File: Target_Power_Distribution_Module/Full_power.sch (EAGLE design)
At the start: 26 parts, among them IC1 MCP1702, Q1 NFET, Q2 PFET, Q3 NFET, Q4 PFET

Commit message: Initial .brd done for power
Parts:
- removed BAT1: 5V, SparkFun-Connectors:BC9VPC
- removed U$1: USB-CON-5PIN-105017-0001, GeekAmmo:USB-CON-5PIN-105017-0001
- added JP1: USB-MICROB, SparkFun-Connectors:USB-MICROB
- added PI, SENSOR, STATE_CONTROLLER: (no value), SparkFun-Connectors:M02PTH
- C1: device SparkFun-Capacitors:CAP1206 -> SparkFun-Passives:CAPPTH
- D1: device adafruit:SCHOTTKY-DIODECB429-15 -> SparkFun-DiscreteSemi:DIODEPTH
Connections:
- net 5V: now also STATE_CONTROLLER.1
- net 5V_RAW: now also JP1.VBUS; no longer BAT1.V+, U$1.VBUS
- net GND-ISO: now also JP1.GND, PI.2, SENSOR.2, STATE_CONTROLLER.2; no longer BAT1.V-, U$1.GND
- net PI_5V: now also PI.1
- net SENSOR_POWER: now also SENSOR.1
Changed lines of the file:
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@@
 <part name="R2" library="SparkFun-Resistors" deviceset="RESISTOR" device="1206" value="10k"/>
 <part name="R3" library="SparkFun-Resistors" deviceset="RESISTOR" device="1206" value="10k"/>
-<part name="D1" library="adafruit" deviceset="SCHOTTKY-DIODE" device="CB429-15" value="1N5817"/>
+<part name="D1" library="SparkFun-DiscreteSemi" deviceset="DIODE" device="PTH" value="1N5817"/>
 <part name="F1" library="fuse" deviceset="FUSE" device="PICOFUSE" value="2A"/>
 <part name="Q3" library="User-Submitted" deviceset="MOSFET-PCHANNEL" device="FQP27P06" value="NFET"/>
@@
 <part name="R6" library="SparkFun-Resistors" deviceset="RESISTOR" device="1206" value="10k"/>
 <part name="GND-ISO2" library="SparkFun-Aesthetics" deviceset="GND-ISO" device=""/>
-<part name="BAT1" library="SparkFun-Connectors" deviceset="BC9VPC" device="" value="5V"/>
-<part name="GND-ISO3" library="SparkFun-Aesthetics" deviceset="GND-ISO" device=""/>
-<part name="5V_RAW" library="SparkFun-Aesthetics" deviceset="VCC" device="" value="5V_RAW"/>
 <part name="5V_RAW1" library="SparkFun-Aesthetics" deviceset="VCC" device="" value="5V_RAW"/>
 <part name="SW1" library="special" deviceset="SW_DIP-1" device=""/>
-<part name="U$1" library="GeekAmmo" deviceset="USB-CON-5PIN" device="-105017-0001"/>
 <part name="D2" library="SparkFun-DiscreteSemi" deviceset="DIODE-ZENER" device="PTH" value="TVS"/>
 <part name="F3" library="fuse" deviceset="PICOFUSE" device="" value="FUSE (3.5A)"/>
 <part name="F4" library="SparkFun-PowerIC" deviceset="PTC" device="PTH" value="PTC (1.5A)"/>
-<part name="C1" library="SparkFun-Capacitors" deviceset="CAP" device="1206" value=".1 uF"/>
+<part name="C1" library="SparkFun-Passives" deviceset="CAP" device="PTH" value=".1 uF"/>
 <part name="C2" library="SparkFun-Passives" deviceset="CAP_POL" device="PTH2" value="10 uF"/>
 <part name="GND-ISO5" library="SparkFun-Aesthetics" deviceset="GND-ISO" device=""/>
@@
 <part name="SW2" library="special" deviceset="SW_DIP-1" device=""/>
 <part name="SW3" library="special" deviceset="SW_DIP-1" device=""/>
+<part name="PI" library="SparkFun-Connectors" deviceset="M02" device="PTH"/>
+<part name="SENSOR" library="SparkFun-Connectors" deviceset="M02" device="PTH"/>
+<part name="STATE_CONTROLLER" library="SparkFun-Connectors" deviceset="M02" device="PTH"/>
+<part name="GND-ISO3" library="SparkFun-Aesthetics" deviceset="GND-ISO" device=""/>
+<part name="GND-ISO4" library="SparkFun-Aesthetics" deviceset="GND-ISO" device=""/>
+<part name="GND-ISO7" library="SparkFun-Aesthetics" deviceset="GND-ISO" device=""/>
+<part name="JP1" library="SparkFun-Connectors" deviceset="USB" device="-MICROB"/>
 </parts>
 <sheets>
@@
 <instance part="R6" gate="G$1" x="5.08" y="50.8" rot="R90"/>
 <instance part="GND-ISO2" gate="G$1" x="-15.24" y="15.24"/>
-<instance part="BAT1" gate="G$1" x="-238.76" y="-27.94"/>
-<instance part="GND-ISO3" gate="G$1" x="-238.76" y="-48.26"/>
-<instance part="5V_RAW" gate="G$1" x="-238.76" y="-10.16"/>
 <instance part="5V_RAW1" gate="G$1" x="-185.42" y="-15.24"/>
 <instance part="SW1" gate="G$1" x="-172.72" y="-20.32"/>
-<instance part="U$1" gate="G$1" x="-215.9" y="-27.94"/>
 <instance part="D2" gate="G$1" x="-111.76" y="-38.1" smashed="yes" rot="R90">
 <attribute name="NAME" x="-114.7826" y="-40.64" size="1.778" layer="95" rot="R90"/>
@@
 <instance part="SW2" gate="G$1" x="-152.4" y="68.58"/>
 <instance part="SW3" gate="G$1" x="20.32" y="63.5"/>
+<instance part="PI" gate="G$1" x="116.84" y="5.08" rot="R180"/>
+<instance part="SENSOR" gate="G$1" x="116.84" y="-17.78" rot="R180"/>
+<instance part="STATE_CONTROLLER" gate="G$1" x="116.84" y="-38.1" smashed="yes" rot="R180">
+<attribute name="VALUE" x="119.38" y="-33.02" size="1.778" layer="96" rot="R180"/>
+<attribute name="NAME" x="134.62" y="-43.942" size="1.778" layer="95" rot="R180"/>
+</instance>
+<instance part="GND-ISO3" gate="G$1" x="88.9" y="-2.54"/>
+<instance part="GND-ISO4" gate="G$1" x="88.9" y="-25.4"/>
+<instance part="GND-ISO7" gate="G$1" x="88.9" y="-45.72"/>
+<instance part="JP1" gate="G$1" x="-210.82" y="-30.48" rot="MR0"/>
 </instances>
 <busses>
@@
 </segment>
 <segment>
-<pinref part="BAT1" gate="G$1" pin="V-"/>
-<wire x1="-238.76" y1="-38.1" x2="-238.76" y2="-45.72" width="0.1524" layer="91"/>
-<pinref part="GND-ISO3" gate="G$1" pin="GND-ISO"/>
-</segment>
-<segment>
 <pinref part="C1" gate="G$1" pin="2"/>
 <wire x1="-86.36" y1="-43.18" x2="-86.36" y2="-48.26" width="0.1524" layer="91"/>
-<pinref part="D2" gate="G$1" pin="A"/>
 <wire x1="-86.36" y1="-48.26" x2="-99.06" y2="-48.26" width="0.1524" layer="91"/>
-<wire x1="-99.06" y1="-48.26" x2="-111.76" y2="-48.26" width="0.1524" layer="91"/>
-<wire x1="-111.76" y1="-48.26" x2="-111.76" y2="-40.64" width="0.1524" layer="91"/>
 <pinref part="C2" gate="G$1" pin="-"/>
 <wire x1="-99.06" y1="-43.18" x2="-99.06" y2="-48.26" width="0.1524" layer="91"/>
 <junction x="-99.06" y="-48.26"/>
+<wire x1="-99.06" y1="-48.26" x2="-111.76" y2="-48.26" width="0.1524" layer="91"/>
+<pinref part="GND-ISO5" gate="G$1" pin="GND-ISO"/>
 <wire x1="-111.76" y1="-48.26" x2="-157.48" y2="-48.26" width="0.1524" layer="91"/>
-<junction x="-111.76" y="-48.26"/>
-<pinref part="GND-ISO5" gate="G$1" pin="GND-ISO"/>
 <wire x1="-157.48" y1="-55.88" x2="-157.48" y2="-48.26" width="0.1524" layer="91"/>
 <junction x="-86.36" y="-48.26"/>
-<pinref part="U$1" gate="G$1" pin="GND"/>
-<wire x1="-205.74" y1="-33.02" x2="-198.12" y2="-33.02" width="0.1524" layer="91"/>
-<wire x1="-198.12" y1="-33.02" x2="-198.12" y2="-30.48" width="0.1524" layer="91"/>
-<wire x1="-198.12" y1="-30.48" x2="-185.42" y2="-30.48" width="0.1524" layer="91"/>
+<wire x1="-208.28" y1="-30.48" x2="-185.42" y2="-30.48" width="0.1524" layer="91"/>
 <wire x1="-185.42" y1="-30.48" x2="-185.42" y2="-48.26" width="0.1524" layer="91"/>
 <wire x1="-185.42" y1="-48.26" x2="-157.48" y2="-48.26" width="0.1524" layer="91"/>
@@
 <wire x1="-30.48" y1="-40.64" x2="-30.48" y2="-48.26" width="0.1524" layer="91"/>
 <wire x1="-30.48" y1="-48.26" x2="-43.18" y2="-48.26" width="0.1524" layer="91"/>
+<pinref part="D2" gate="G$1" pin="A"/>
+<wire x1="-111.76" y1="-40.64" x2="-111.76" y2="-48.26" width="0.1524" layer="91"/>
+<junction x="-111.76" y="-48.26"/>
+<pinref part="JP1" gate="G$1" pin="GND"/>
+</segment>
+<segment>
+<pinref part="PI" gate="G$1" pin="2"/>
+<wire x1="109.22" y1="2.54" x2="88.9" y2="2.54" width="0.1524" layer="91"/>
+<pinref part="GND-ISO3" gate="G$1" pin="GND-ISO"/>
+<wire x1="88.9" y1="2.54" x2="88.9" y2="0" width="0.1524" layer="91"/>
+</segment>
+<segment>
+<pinref part="SENSOR" gate="G$1" pin="2"/>
+<wire x1="109.22" y1="-20.32" x2="88.9" y2="-20.32" width="0.1524" layer="91"/>
+<pinref part="GND-ISO4" gate="G$1" pin="GND-ISO"/>
+<wire x1="88.9" y1="-20.32" x2="88.9" y2="-22.86" width="0.1524" layer="91"/>
+</segment>
+<segment>
+<pinref part="STATE_CONTROLLER" gate="G$1" pin="2"/>
+<wire x1="109.22" y1="-40.64" x2="88.9" y2="-40.64" width="0.1524" layer="91"/>
+<pinref part="GND-ISO7" gate="G$1" pin="GND-ISO"/>
+<wire x1="88.9" y1="-40.64" x2="88.9" y2="-43.18" width="0.1524" layer="91"/>
 </segment>
 </net>
@@
 <wire x1="-111.76" y1="30.48" x2="-99.06" y2="30.48" width="0.1524" layer="91"/>
 <label x="-99.06" y="30.48" size="1.778" layer="95" xref="yes"/>
+</segment>
+<segment>
+<pinref part="PI" gate="G$1" pin="1"/>
+<wire x1="109.22" y1="5.08" x2="91.44" y2="5.08" width="0.1524" layer="91"/>
+<label x="91.44" y="5.08" size="1.27" layer="95" rot="R180" xref="yes"/>
 </segment>
 </net>
@@
 <label x="-76.2" y="-20.32" size="1.778" layer="95" rot="R90" xref="yes"/>
 </segment>
+<segment>
+<pinref part="STATE_CONTROLLER" gate="G$1" pin="1"/>
+<wire x1="109.22" y1="-38.1" x2="91.44" y2="-38.1" width="0.1524" layer="91"/>
+<label x="91.44" y="-38.1" size="1.27" layer="95" rot="R180" xref="yes"/>
+</segment>
 </net>
 <net name="SENSOR_PWR_CNTRL" class="0">
@@
 <label x="60.96" y="33.02" size="1.778" layer="95" xref="yes"/>
 </segment>
+<segment>
+<pinref part="SENSOR" gate="G$1" pin="1"/>
+<wire x1="109.22" y1="-17.78" x2="91.44" y2="-17.78" width="0.1524" layer="91"/>
+<label x="91.44" y="-17.78" size="1.27" layer="95" rot="R180" xref="yes"/>
+</segment>
 </net>
 <net name="N$7" class="0">
@@
 </net>
 <net name="5V_RAW" class="0">
-<segment>
-<pinref part="BAT1" gate="G$1" pin="V+"/>
-<wire x1="-238.76" y1="-20.32" x2="-238.76" y2="-10.16" width="0.1524" layer="91"/>
-<pinref part="5V_RAW" gate="G$1" pin="VCC"/>
-</segment>
 <segment>
 <wire x1="-185.42" y1="-27.94" x2="-185.42" y2="-15.24" width="0.1524" layer="91"/>
@@
 <pinref part="SW1" gate="G$1" pin="2"/>
 <wire x1="-180.34" y1="-27.94" x2="-180.34" y2="-20.32" width="0.1524" layer="91"/>
-<pinref part="U$1" gate="G$1" pin="VBUS"/>
-<wire x1="-205.74" y1="-22.86" x2="-198.12" y2="-22.86" width="0.1524" layer="91"/>
-<wire x1="-198.12" y1="-22.86" x2="-198.12" y2="-27.94" width="0.1524" layer="91"/>
-<wire x1="-198.12" y1="-27.94" x2="-185.42" y2="-27.94" width="0.1524" layer="91"/>
 <junction x="-185.42" y="-27.94"/>
-</segment>
-</net>
+<pinref part="JP1" gate="G$1" pin="VBUS"/>
+<wire x1="-208.28" y1="-27.94" x2="-185.42" y2="-27.94" width="0.1524" layer="91"/>
+</segment>
+</net>

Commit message: Some schematic updates
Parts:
- removed D2: TVS, SparkFun-DiscreteSemi:DIODE-ZENERPTH
- added CNTRL_INPUTS: (no value), SparkFun-Connectors:M02PTH
- added D3: TVS, SparkFun-DiscreteSemi:DIODEPTH
- C3, C4: value 1 uF -> .1 uF
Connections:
- net 3.3V: now also STATE_CONTROLLER.1
- net 5V: now also D3.C; no longer D2.C, STATE_CONTROLLER.1
- net GND-ISO: now also D3.A; no longer D2.A
- net PI_PWR_CNTRL: now also CNTRL_INPUTS.2
- net SENSOR_PWR_CNTRL: now also CNTRL_INPUTS.1
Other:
- moved on the sheet: C3, D1, F1, F2, PI, Q1, Q2, Q3, Q4, R1, R2, R3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

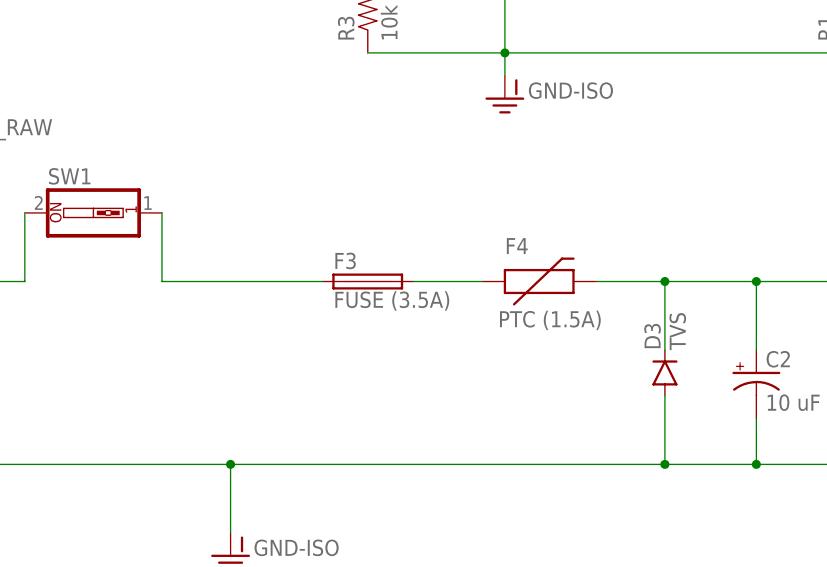
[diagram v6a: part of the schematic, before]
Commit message: Some schematic updates, spi test is working
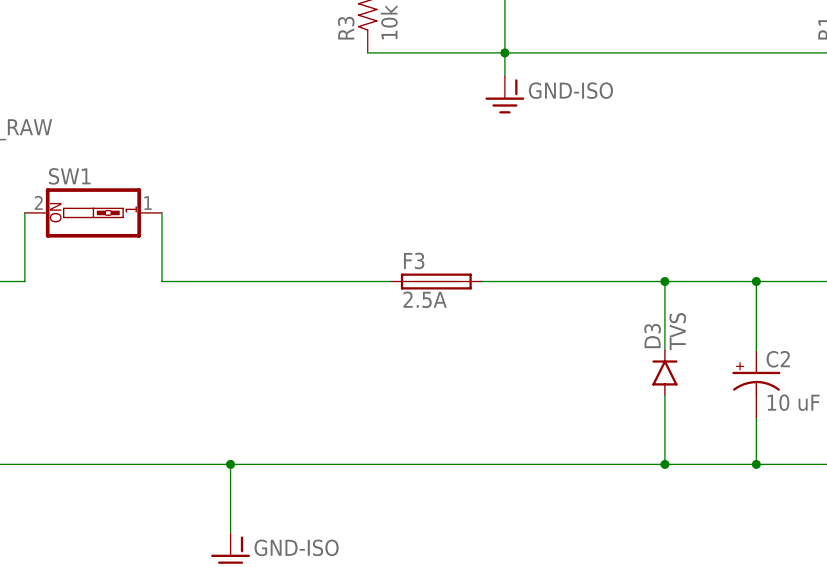
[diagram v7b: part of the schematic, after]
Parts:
- removed F4: PTC (1.5A), SparkFun-PowerIC:PTCPTH
- F3: value FUSE (3.5A) -> 2.5A
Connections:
- removed net N$7: F3.2, F4.1
- net 5V: now also F3.2; no longer F4.2
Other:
- moved on the sheet: F3
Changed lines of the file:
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@@
 <part name="5V_RAW1" library="SparkFun-Aesthetics" deviceset="VCC" device="" value="5V_RAW"/>
 <part name="SW1" library="special" deviceset="SW_DIP-1" device=""/>
-<part name="F3" library="fuse" deviceset="PICOFUSE" device="" value="FUSE (3.5A)"/>
-<part name="F4" library="SparkFun-PowerIC" deviceset="PTC" device="PTH" value="PTC (1.5A)"/>
+<part name="F3" library="fuse" deviceset="PICOFUSE" device="" value="2.5A"/>
 <part name="C1" library="SparkFun-Passives" deviceset="CAP" device="PTH" value=".1 uF"/>
 <part name="C2" library="SparkFun-Passives" deviceset="CAP_POL" device="PTH2" value="10 uF"/>
@@
 <instance part="5V_RAW1" gate="G$1" x="-185.42" y="-15.24"/>
 <instance part="SW1" gate="G$1" x="-172.72" y="-20.32"/>
-<instance part="F3" gate="1" x="-142.24" y="-27.94"/>
-<instance part="F4" gate="G$1" x="-124.46" y="-27.94"/>
+<instance part="F3" gate="1" x="-134.62" y="-27.94"/>
 <instance part="C1" gate="G$1" x="-86.36" y="-40.64"/>
 <instance part="C2" gate="G$1" x="-99.06" y="-38.1"/>
@@
 <pinref part="C4" gate="G$1" pin="1"/>
 <wire x1="-53.34" y1="-33.02" x2="-53.34" y2="-27.94" width="0.1524" layer="91"/>
-<pinref part="F4" gate="G$1" pin="2"/>
 <pinref part="C2" gate="G$1" pin="+"/>
-<wire x1="-116.84" y1="-27.94" x2="-109.22" y2="-27.94" width="0.1524" layer="91"/>
 <wire x1="-109.22" y1="-27.94" x2="-99.06" y2="-27.94" width="0.1524" layer="91"/>
 <wire x1="-99.06" y1="-27.94" x2="-99.06" y2="-35.56" width="0.1524" layer="91"/>
@@
 <wire x1="-109.22" y1="-35.56" x2="-109.22" y2="-27.94" width="0.1524" layer="91"/>
 <junction x="-109.22" y="-27.94"/>
+<pinref part="F3" gate="1" pin="2"/>
+<wire x1="-129.54" y1="-27.94" x2="-109.22" y2="-27.94" width="0.1524" layer="91"/>
 </segment>
 </net>
@@
 </segment>
 </net>
-<net name="N$7" class="0">
-<segment>
-<pinref part="F3" gate="1" pin="2"/>
-<pinref part="F4" gate="G$1" pin="1"/>
-<wire x1="-137.16" y1="-27.94" x2="-129.54" y2="-27.94" width="0.1524" layer="91"/>
-</segment>
-</net>
 <net name="5V_RAW" class="0">
 <segment>
@@
 <segment>
 <pinref part="F3" gate="1" pin="1"/>
-<wire x1="-147.32" y1="-27.94" x2="-165.1" y2="-27.94" width="0.1524" layer="91"/>
+<wire x1="-139.7" y1="-27.94" x2="-165.1" y2="-27.94" width="0.1524" layer="91"/>
 <pinref part="SW1" gate="G$1" pin="1"/>
 <wire x1="-165.1" y1="-20.32" x2="-165.1" y2="-27.94" width="0.1524" layer="91"/>

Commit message: Cleaned sensor on full schem
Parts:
- R1, R2, R3, R4, R5, R6: device SparkFun-Resistors:RESISTOR1206 -> adafruit:R-US_R1206
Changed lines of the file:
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@@
 <part name="Q2" library="User-Submitted" deviceset="MOSFET-PCHANNEL" device="FQP27P06" value="PFET"/>
 <part name="GND-ISO1" library="SparkFun-Aesthetics" deviceset="GND-ISO" device=""/>
-<part name="R1" library="SparkFun-Resistors" deviceset="RESISTOR" device="1206" value="10k"/>
-<part name="R2" library="SparkFun-Resistors" deviceset="RESISTOR" device="1206" value="10k"/>
-<part name="R3" library="SparkFun-Resistors" deviceset="RESISTOR" device="1206" value="10k"/>
+<part name="R1" library="adafruit" deviceset="R-US_" device="R1206" value="10k"/>
+<part name="R2" library="adafruit" deviceset="R-US_" device="R1206" value="10k"/>
+<part name="R3" library="adafruit" deviceset="R-US_" device="R1206" value="10k"/>
 <part name="D1" library="SparkFun-DiscreteSemi" deviceset="DIODE" device="PTH" value="1N5817"/>
 <part name="F1" library="fuse" deviceset="FUSE" device="PICOFUSE" value="2A"/>
@@
 <part name="Q4" library="User-Submitted" deviceset="MOSFET-PCHANNEL" device="FQP27P06" value="PFET"/>
 <part name="F2" library="fuse" deviceset="FUSE" device="PICOFUSE" value="250 mA"/>
-<part name="R4" library="SparkFun-Resistors" deviceset="RESISTOR" device="1206" value="10k"/>
-<part name="R5" library="SparkFun-Resistors" deviceset="RESISTOR" device="1206" value="10k"/>
-<part name="R6" library="SparkFun-Resistors" deviceset="RESISTOR" device="1206" value="10k"/>
+<part name="R4" library="adafruit" deviceset="R-US_" device="R1206" value="10k"/>
+<part name="R5" library="adafruit" deviceset="R-US_" device="R1206" value="10k"/>
+<part name="R6" library="adafruit" deviceset="R-US_" device="R1206" value="10k"/>
 <part name="GND-ISO2" library="SparkFun-Aesthetics" deviceset="GND-ISO" device=""/>
 <part name="5V_RAW1" library="SparkFun-Aesthetics" deviceset="VCC" device="" value="5V_RAW"/>
